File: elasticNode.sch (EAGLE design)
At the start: 135 parts, among them J1 FEMALE_HEADER_2X1, J2 JUMPER, J3 JUMPER, J5 FEMALE_HEADER_10X2, J6 USB_CONNMICRO_SMT, J7 USB_CONNMICRO_SMT, M1 SISS23DN, M2 SISS23DN, M3 SISS23DN, M4 SISS23DN, U1 AT90USB128, U10 LTC3419DFN, U11 PAC1720, U14 LTC3419DFN, U2 IS66WV51216EALL, U3 MRF24J40MA, U4 SPARTAN7-LX15, U5 ATMEGA32U4QFN, U6 SST26VF032BWDFN, U7 PAC1720, U8 PAC1720, U9 PAC1720, X1 8MHz, X2 50MHz, X3 32MHz, X4 100MHz, X5 8MHz

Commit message: backup
SRAM and FPGA finished, now connecting fpga and MCU
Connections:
- new net N$52: U4.IO_L15N_T2_DQS_DOUT_CSO_B_14
- net AD0/SELECTMAP_D7: no longer U4.IO_L5N_T0_D07_14
- net AD1/SELECTMAP_D6: no longer U4.IO_L5P_T0_D06_14
- net AD2/SELECTMAP_D5/MCU_RX1: no longer U4.IO_L4N_T0_D05_14
- net AD3/SELECTMAP_D4/MCU_TX1: no longer U4.IO_L4P_T0_D04_14
- net AD4/SELECTMAP_D3/FPGA_HOLD: no longer U4.IO_L2N_T0_D03_14
- net AD5/SELECTMAP_D2/FPGA_WP: no longer U4.IO_L2P_T0_D02_14
- net AD6/SELECTMAP_D1/SPI_MISO/MCU_PDO: no longer U4.IO_L1N_T0_D01_DIN_14
- net AD7/SELECTMAP_D0/SPI_MOSI/PDI: no longer U4.IO_L1P_T0_D00_MOSI_14
- net ALE/HWB: no longer U4.IO_L12P_T1_MRCC_14
- net FPGA_LED0: no longer U4.IO_0_14
- net FPGA_LED1: no longer U4.IO_L3P_T0_DQS_PUDC_B_14
- net FPGA_LED2: no longer U4.IO_L3N_T0_DQS_EMCCLK_14
- net FPGA_LED3: no longer U4.IO_L6N_T0_D08_VREF_14
- net SPI_CS: no longer U4.IO_L15N_T2_DQS_DOUT_CSO_B_14, U4.IO_L6P_T0_FCS_B_14
- net SRAM_A0: now also U4.IO_L5P_T0_34
- net SRAM_A1: now also U4.IO_L3P_T0_DQS_34
- net SRAM_A12: now also U4.IO_L24P_T3_34
- net SRAM_A13: now also U4.IO_L21P_T3_DQS_34
- net SRAM_A14: now also U4.IO_L21N_T3_DQS_34
- net SRAM_A15: now also U4.IO_L20P_T3_34
- net SRAM_A16: now also U4.IO_L17P_T2_34
- net SRAM_A2: now also U4.IO_L4P_T0_34
- net SRAM_A3: now also U4.IO_0_34
- net SRAM_CS: now also U4.IO_L6N_T0_VREF_34
- net SRAM_D0: now also U4.IO_L1N_T0_34
- net SRAM_D1: now also U4.IO_L10N_T1_34
- net SRAM_D2: now also U4.IO_L1P_T0_34
- net SRAM_D3: now also U4.IO_L10P_T1_34
- net SRAM_D4: now also U4.IO_L8N_T1_34
- net SRAM_D5: now also U4.IO_L8P_T1_34
- net SRAM_D6: now also U4.IO_L13P_T2_MRCC_34
- net SRAM_D7: now also U4.IO_L14P_T2_SRCC_34
- net SRAM_WE: now also U4.IO_L13N_T2_MRCC_34
- net XMEM_A10: now also U4.IO_L5P_T0_D06_14; no longer U4.IO_L10N_T1_D15_14
- net XMEM_A11: no longer U4.IO_L8N_T1_D12_14
- net XMEM_A12: now also U4.IO_L11N_T1_SRCC_14, U4.IO_L6N_T0_D08_VREF_14; no longer U4.IO_L9P_T1_DQS_14
- net XMEM_A13: now also U4.IO_L8P_T1_D11_14; no longer U4.IO_L9N_T1_DQS_D13_14
- net XMEM_A14: no longer U4.IO_L10P_T1_D14_14
- net XMEM_A15: no longer U4.IO_L7P_T1_D09_14
- net XMEM_A8: now also U4.IO_L1N_T0_D01_DIN_14; no longer U4.IO_L7N_T1_D10_14
- net XMEM_A9: now also U4.IO_L5N_T0_D07_14; no longer U4.IO_L8P_T1_D11_14
- net XMEM_RD: now also U4.IO_L4N_T0_D05_14; no longer U4.IO_L11N_T1_SRCC_14
- net XMEM_WR: now also U4.IO_L4P_T0_D04_14; no longer U4.IO_L11P_T1_SRCC_14

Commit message: back up
spi_sck didn’t connect to FPGA,OK？
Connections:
- net AD6/SELECTMAP_D1/SPI_MISO/MCU_PDO: now also U4.IO_L1N_T0_D01_DIN_14
- net AD7/SELECTMAP_D0/SPI_MOSI/PDI: now also U4.IO_L1P_T0_D00_MOSI_14
- net FPGA_LED0: now also U4.IO_L2P_T0_D02_14
- net FPGA_LED1: now also U4.IO_L2N_T0_D03_14
- net FPGA_LED2: now also U4.IO_L3P_T0_DQS_PUDC_B_14
- net FPGA_LED3: now also U4.IO_L3N_T0_DQS_EMCCLK_14
- net XMEM_A10: no longer U4.IO_L5P_T0_D06_14
- net XMEM_A12: no longer U4.IO_L11N_T1_SRCC_14, U4.IO_L6N_T0_D08_VREF_14
- net XMEM_A13: no longer U4.IO_L8P_T1_D11_14
- net XMEM_A8: no longer U4.IO_L1N_T0_D01_DIN_14
- net XMEM_A9: no longer U4.IO_L5N_T0_D07_14

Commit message: backup
SPI FLASH ok.
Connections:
- removed net N$52: U4.IO_L15N_T2_DQS_DOUT_CSO_B_14
- net AD0/SELECTMAP_D7: now also U4.IO_L5N_T0_D07_14
- net AD1/SELECTMAP_D6: now also U4.IO_L5P_T0_D06_14
- net AD2/SELECTMAP_D5/MCU_RX1: now also U4.IO_L4N_T0_D05_14
- net AD3/SELECTMAP_D4/MCU_TX1: now also U4.IO_L4P_T0_D04_14
- net AD4/SELECTMAP_D3/FPGA_HOLD: now also U4.IO_L2N_T0_D03_14
- net AD5/SELECTMAP_D2/FPGA_WP: now also U4.IO_L2P_T0_D02_14
- net FPGA_LED0: now also U4.IO_0_14; no longer U4.IO_L2P_T0_D02_14
- net FPGA_LED1: now also U4.IO_L3P_T0_DQS_PUDC_B_14; no longer U4.IO_L2N_T0_D03_14
- net FPGA_LED2: now also U4.IO_L3N_T0_DQS_EMCCLK_14; no longer U4.IO_L3P_T0_DQS_PUDC_B_14
- net FPGA_LED3: no longer U4.IO_L3N_T0_DQS_EMCCLK_14
- net SPI_CS: now also U4.IO_L6P_T0_FCS_B_14
- net XMEM_RD: no longer U4.IO_L4N_T0_D05_14
- net XMEM_WR: no longer U4.IO_L4P_T0_D04_14

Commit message: backup
FPGA_GPIO connecting
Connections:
- new net N$1: U4.IO_L24N_T3_D16_14
- new net N$31: U4.IO_L22N_T3_D20_14
- new net N$32: U4.IO_L22P_T3_D21_14
- new net N$35: U4.IO_L15N_T2_DQS_DOUT_CSO_B_14
- new net N$36: U4.IO_L21N_T3_DQS_D22_14
- new net N$37: U4.IO_L21P_T3_DQS_14
- new net N$8: U4.IO_L24P_T3_D17_14
- net ALE/HWB: now also U4.IO_L9P_T1_DQS_14
- net FPGA_GPIO_0: now also U4.IO_L13N_T2_MRCC_14; no longer U4.IO_L22N_T3_D20_14
- net FPGA_GPIO_1: no longer U4.IO_L22P_T3_D21_14
- net FPGA_GPIO_10: no longer U4.IO_25_14
- net FPGA_GPIO_11: now also U4.IO_L18P_T2_D28_14; no longer U4.IO_L16N_T2_D31_14
- net FPGA_GPIO_12: no longer U4.IO_L19N_T3_D25_VREF_14
- net FPGA_GPIO_13: now also U4.IO_L18N_T2_D27_14; no longer U4.IO_L19P_T3_D26_14
- net FPGA_GPIO_14: now also U4.IO_L19P_T3_D26_14; no longer U4.IO_L18N_T2_D27_14
- net FPGA_GPIO_15: no longer U4.IO_L18P_T2_D28_14
- net FPGA_GPIO_16: now also U4.IO_L19N_T3_D25_VREF_14; no longer U4.IO_L17N_T2_D29_14
- net FPGA_GPIO_17: no longer U4.IO_L17P_T2_D30_14
- net FPGA_GPIO_18: no longer U4.IO_L14N_T2_SRCC_14
- net FPGA_GPIO_19: no longer U4.IO_L14P_T2_SRCC_14
- net FPGA_GPIO_2: now also U4.IO_L14P_T2_SRCC_14; no longer U4.IO_L24N_T3_D16_14
- net FPGA_GPIO_3: no longer U4.IO_L24P_T3_D17_14
- net FPGA_GPIO_4: now also U4.IO_L14N_T2_SRCC_14; no longer U4.IO_L21P_T3_DQS_14
- net FPGA_GPIO_5: no longer U4.IO_L23N_T3_D18_14
- net FPGA_GPIO_6: now also U4.IO_L17P_T2_D30_14; no longer U4.IO_L23P_T3_D19_14
- net FPGA_GPIO_7: no longer U4.IO_L21N_T3_DQS_D22_14
- net FPGA_GPIO_8: now also U4.IO_L17N_T2_D29_14; no longer U4.IO_L20N_T3_D23_14
- net FPGA_GPIO_9: no longer U4.IO_L20P_T3_D24_14
- net FPGA_LED3: now also U4.IO_L6N_T0_D08_VREF_14
- net XMEM_A10: now also U4.IO_L7N_T1_D10_14
- net XMEM_A11: now also U4.IO_L10N_T1_D15_14
- net XMEM_A12: now also U4.IO_L7P_T1_D09_14
- net XMEM_A13: now also U4.IO_L10P_T1_D14_14
- net XMEM_A14: now also U4.IO_L9N_T1_DQS_D13_14
- net XMEM_A15: now also U4.IO_L12P_T1_MRCC_14
- net XMEM_A8: now also U4.IO_L8N_T1_D12_14
- net XMEM_A9: now also U4.IO_L11P_T1_SRCC_14
- net XMEM_RD: now also U4.IO_L8P_T1_D11_14
- net XMEM_WR: now also U4.IO_L11N_T1_SRCC_14

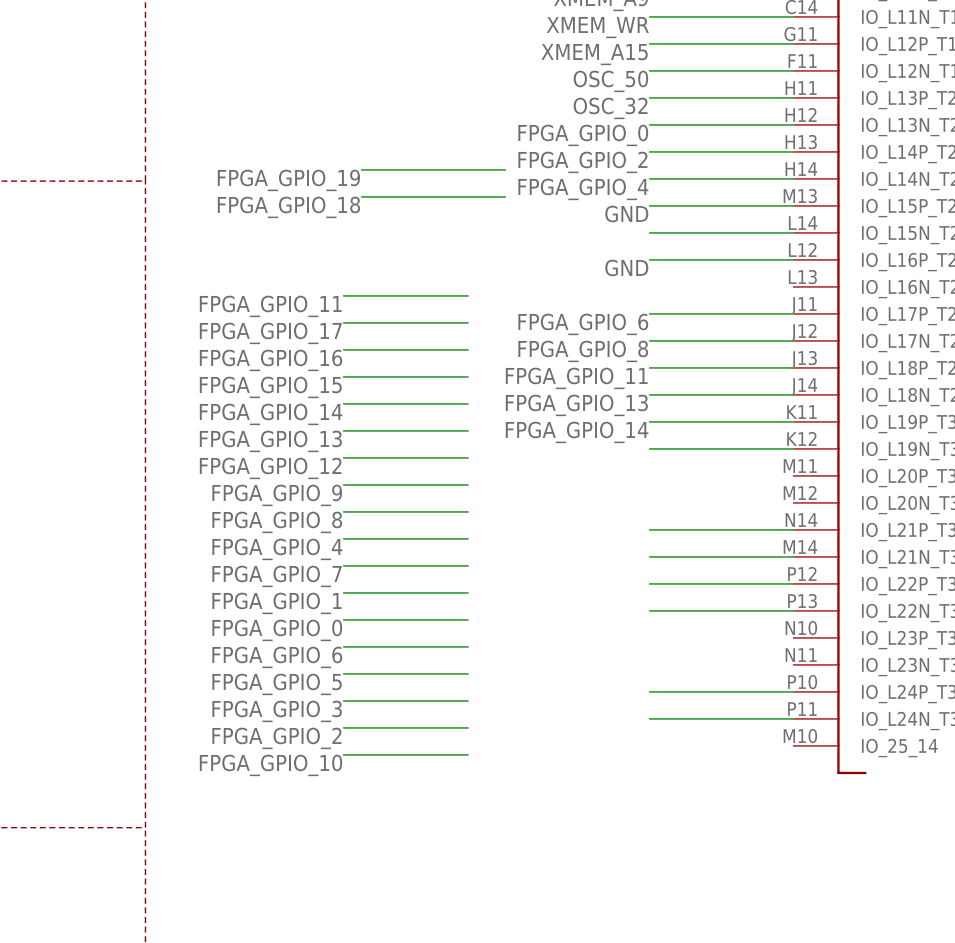
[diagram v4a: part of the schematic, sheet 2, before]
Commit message: back up
power line need check again.
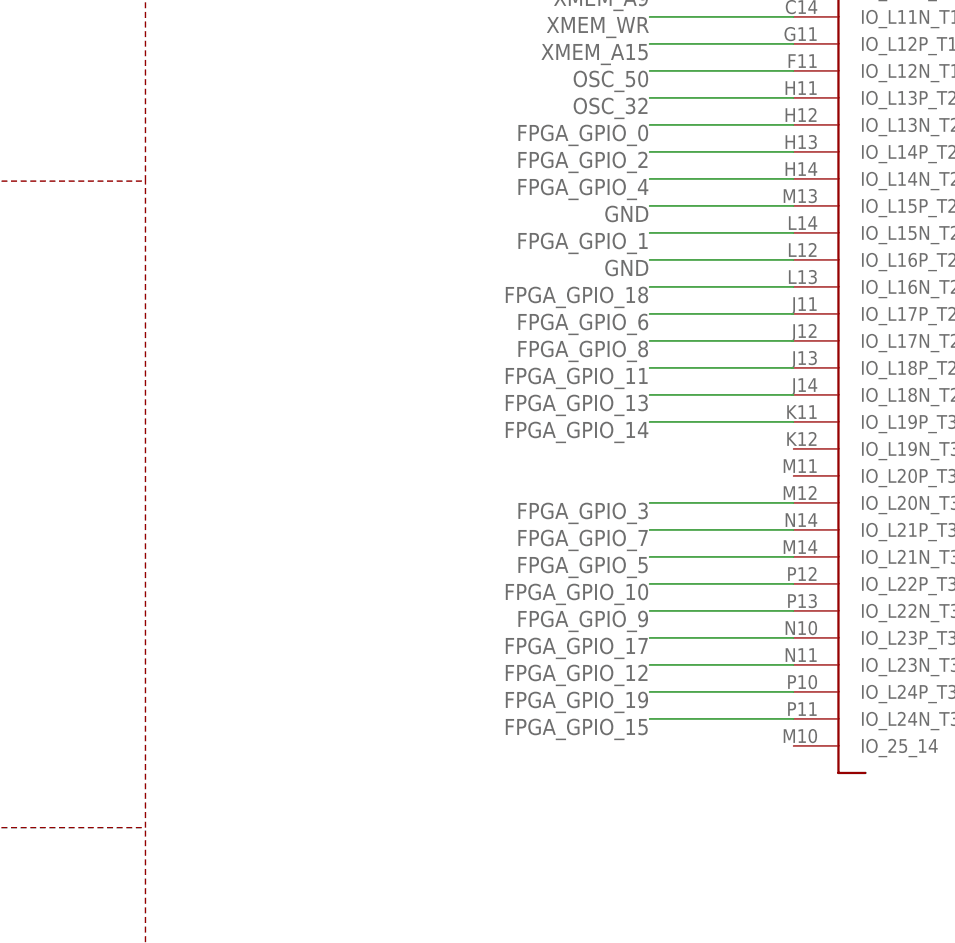
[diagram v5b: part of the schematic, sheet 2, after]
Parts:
- added R39: 2.4k, passive:RESISTOR
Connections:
- removed net N$1: U4.IO_L24N_T3_D16_14
- removed net N$31: U4.IO_L22N_T3_D20_14
- removed net N$32: U4.IO_L22P_T3_D21_14
- removed net N$35: U4.IO_L15N_T2_DQS_DOUT_CSO_B_14
- removed net N$36: U4.IO_L21N_T3_DQS_D22_14
- removed net N$37: U4.IO_L21P_T3_DQS_14
- removed net N$8: U4.IO_L24P_T3_D17_14
- net 3V3: now also R39.1
- net FPGA_GPIO_1: now also U4.IO_L15N_T2_DQS_DOUT_CSO_B_14
- net FPGA_GPIO_10: now also U4.IO_L22P_T3_D21_14
- net FPGA_GPIO_12: now also U4.IO_L23N_T3_D18_14
- net FPGA_GPIO_15: now also U4.IO_L24N_T3_D16_14
- net FPGA_GPIO_16: no longer U4.IO_L19N_T3_D25_VREF_14
- net FPGA_GPIO_17: now also U4.IO_L23P_T3_D19_14
- net FPGA_GPIO_18: now also U4.IO_L16N_T2_D31_14
- net FPGA_GPIO_19: now also U4.IO_L24P_T3_D17_14
- net FPGA_GPIO_3: now also U4.IO_L20N_T3_D23_14
- net FPGA_GPIO_5: now also U4.IO_L21N_T3_DQS_D22_14
- net FPGA_GPIO_7: now also U4.IO_L21P_T3_DQS_14
- net FPGA_GPIO_9: now also U4.IO_L22N_T3_D20_14
- net MONITORING: now also R39.2
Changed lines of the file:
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@@
 <part name="C30" library="passive" deviceset="CAPACITOR" device="0805" value="4.7u"/>
 <part name="C32" library="passive" deviceset="CAPACITOR" device="0805" value="0.47u"/>
+<part name="R39" library="passive" deviceset="RESISTOR" device="" value="2.4k"/>
 </parts>
 <sheets>
@@
 <attribute name="VALUE" x="9" y="-174" size="1.778" layer="96" align="top-center"/>
 </instance>
+<instance part="R39" gate="G$1" x="-141" y="-205" smashed="yes" rot="R90">
+<attribute name="NAME" x="-143" y="-205" size="1.778" layer="95" rot="R90" align="bottom-center"/>
+<attribute name="VALUE" x="-139" y="-205" size="1.778" layer="96" rot="R90" align="top-center"/>
+</instance>
 </instances>
 <busses>
@@
 <label x="169" y="-151" size="1.778" layer="95"/>
 </segment>
+<segment>
+<wire x1="-141" y1="-209.46" x2="-141" y2="-213" width="0.1524" layer="91"/>
+<label x="-141" y="-213" size="1.778" layer="95"/>
+<pinref part="R39" gate="G$1" pin="1"/>
+</segment>
 </net>
 <net name="INIT_B" class="0">
@@
 <segment>
 <pinref part="U5" gate="G$1" pin="PE6(INT6/AIN0)"/>
-<wire x1="-137" y1="-197" x2="-145" y2="-197" width="0.1524" layer="91"/>
 <label x="-145" y="-197" size="1.778" layer="95" rot="R180"/>
+<wire x1="-137" y1="-197" x2="-141" y2="-197" width="0.1524" layer="91"/>
+<wire x1="-141" y1="-197" x2="-145" y2="-197" width="0.1524" layer="91"/>
+<wire x1="-141" y1="-200.54" x2="-141" y2="-197" width="0.1524" layer="91"/>
+<junction x="-141" y="-197"/>
+<pinref part="R39" gate="G$1" pin="2"/>
 </segment>
 <segment>
@@
 </segment>
 <segment>
-<label x="-97" y="-62" size="1.778" layer="95" rot="R180"/>
-<wire x1="-83.1524" y1="-62" x2="-97" y2="-62" width="0.1524" layer="91"/>
-</segment>
-<segment>
 <pinref part="U4" gate="G$1" pin="IO_L13N_T2_MRCC_14"/>
 <wire x1="-47" y1="-7" x2="-63" y2="-7" width="0.1524" layer="91"/>
@@
 </segment>
 <segment>
-<label x="-97" y="-59" size="1.778" layer="95" rot="R180"/>
-<wire x1="-83.1524" y1="-59" x2="-97" y2="-59" width="0.1524" layer="91"/>
+<pinref part="U4" gate="G$1" pin="IO_L15N_T2_DQS_DOUT_CSO_B_14"/>
+<wire x1="-47" y1="-19" x2="-63" y2="-19" width="0.1524" layer="91"/>
+<label x="-63" y="-19" size="1.778" layer="95" rot="R180"/>
 </segment>
 </net>
@@
 </segment>
 <segment>
-<label x="-97" y="-74" size="1.778" layer="95" rot="R180"/>
-<wire x1="-83.1524" y1="-74" x2="-97" y2="-74" width="0.1524" layer="91"/>
-</segment>
-<segment>
 <pinref part="U4" gate="G$1" pin="IO_L14P_T2_SRCC_14"/>
 <wire x1="-47" y1="-10" x2="-63" y2="-10" width="0.1524" layer="91"/>
@@
 </segment>
 <segment>
-<label x="-97" y="-71" size="1.778" layer="95" rot="R180"/>
-<wire x1="-83.1524" y1="-71" x2="-97" y2="-71" width="0.1524" layer="91"/>
+<pinref part="U4" gate="G$1" pin="IO_L20N_T3_D23_14"/>
+<wire x1="-47" y1="-49" x2="-63" y2="-49" width="0.1524" layer="91"/>
+<label x="-63" y="-49" size="1.778" layer="95" rot="R180"/>
 </segment>
 </net>
@@
 </segment>
 <segment>
-<label x="-97" y="-53" size="1.778" layer="95" rot="R180"/>
-<wire x1="-83.1524" y1="-53" x2="-97" y2="-53" width="0.1524" layer="91"/>
-</segment>
-<segment>
 <pinref part="U4" gate="G$1" pin="IO_L14N_T2_SRCC_14"/>
 <wire x1="-47" y1="-13" x2="-63" y2="-13" width="0.1524" layer="91"/>
@@
 </segment>
 <segment>
-<label x="-97" y="-68" size="1.778" layer="95" rot="R180"/>
-<wire x1="-83.1524" y1="-68" x2="-97" y2="-68" width="0.1524" layer="91"/>
+<pinref part="U4" gate="G$1" pin="IO_L21N_T3_DQS_D22_14"/>
+<wire x1="-47" y1="-55" x2="-63" y2="-55" width="0.1524" layer="91"/>
+<label x="-63" y="-55" size="1.778" layer="95" rot="R180"/>
 </segment>
 </net>
@@
 </segment>
 <segment>
-<label x="-97" y="-65" size="1.778" layer="95" rot="R180"/>
-<wire x1="-83.1524" y1="-65" x2="-97" y2="-65" width="0.1524" layer="91"/>
-</segment>
-<segment>
 <pinref part="U4" gate="G$1" pin="IO_L17P_T2_D30_14"/>
 <wire x1="-47" y1="-28" x2="-63" y2="-28" width="0.1524" layer="91"/>
@@
 </segment>
 <segment>
-<label x="-97" y="-56" size="1.778" layer="95" rot="R180"/>
-<wire x1="-83.1524" y1="-56" x2="-97" y2="-56" width="0.1524" layer="91"/>
+<pinref part="U4" gate="G$1" pin="IO_L21P_T3_DQS_14"/>
+<wire x1="-47" y1="-52" x2="-63" y2="-52" width="0.1524" layer="91"/>
+<label x="-63" y="-52" size="1.778" layer="95" rot="R180"/>
 </segment>
 </net>
@@
 </segment>
 <segment>
-<label x="-97" y="-50" size="1.778" layer="95" rot="R180"/>
-<wire x1="-83.1524" y1="-50" x2="-97" y2="-50" width="0.1524" layer="91"/>
-</segment>
-<segment>
 <pinref part="U4" gate="G$1" pin="IO_L17N_T2_D29_14"/>
 <wire x1="-47" y1="-31" x2="-63" y2="-31" width="0.1524" layer="91"/>
@@
 </segment>
 <segment>
-<label x="-97" y="-47" size="1.778" layer="95" rot="R180"/>
-<wire x1="-83.1524" y1="-47" x2="-97" y2="-47" width="0.1524" layer="91"/>
+<pinref part="U4" gate="G$1" pin="IO_L22N_T3_D20_14"/>
+<wire x1="-47" y1="-61" x2="-63" y2="-61" width="0.1524" layer="91"/>
+<label x="-63" y="-61" size="1.778" layer="95" rot="R180"/>
 </segment>
 </net>
@@
 </segment>
 <segment>
-<label x="-97" y="-77" size="1.778" layer="95" rot="R180"/>
-<wire x1="-83.1524" y1="-77" x2="-97" y2="-77" width="0.1524" layer="91"/>
+<pinref part="U4" gate="G$1" pin="IO_L22P_T3_D21_14"/>
+<wire x1="-47" y1="-58" x2="-63" y2="-58" width="0.1524" layer="91"/>
+<label x="-63" y="-58" size="1.778" layer="95" rot="R180"/>
 </segment>
 </net>
@@
 </segment>
 <segment>
-<label x="-97" y="-26" size="1.778" layer="95" rot="R180"/>
-<wire x1="-83.1524" y1="-26" x2="-97" y2="-26" width="0.1524" layer="91"/>
-</segment>
-<segment>
 <pinref part="U4" gate="G$1" pin="IO_L18P_T2_D28_14"/>
 <wire x1="-47" y1="-34" x2="-63" y2="-34" width="0.1524" layer="91"/>
@@
 </segment>
 <segment>
-<label x="-97" y="-44" size="1.778" layer="95" rot="R180"/>
-<wire x1="-83.1524" y1="-44" x2="-97" y2="-44" width="0.1524" layer="91"/>
+<pinref part="U4" gate="G$1" pin="IO_L23N_T3_D18_14"/>
+<wire x1="-47" y1="-67" x2="-63" y2="-67" width="0.1524" layer="91"/>
+<label x="-63" y="-67" size="1.778" layer="95" rot="R180"/>
 </segment>
 </net>
@@
 </segment>
 <segment>
-<label x="-97" y="-41" size="1.778" layer="95" rot="R180"/>
-<wire x1="-83.1524" y1="-41" x2="-97" y2="-41" width="0.1524" layer="91"/>
-</segment>
-<segment>
 <pinref part="U4" gate="G$1" pin="IO_L18N_T2_D27_14"/>
 <wire x1="-47" y1="-37" x2="-63" y2="-37" width="0.1524" layer="91"/>
@@
 </segment>
 <segment>
-<label x="-97" y="-35" size="1.778" layer="95" rot="R180"/>
-<wire x1="-83.1524" y1="-35" x2="-97" y2="-35" width="0.1524" layer="91"/>
+<pinref part="U4" gate="G$1" pin="IO_L24N_T3_D16_14"/>
+<wire x1="-47" y1="-73" x2="-63" y2="-73" width="0.1524" layer="91"/>
+<label x="-63" y="-73" size="1.778" layer="95" rot="R180"/>
 </segment>
 </net>
@@
 </segment>
 <segment>
-<label x="-97" y="-29" size="1.778" layer="95" rot="R180"/>
-<wire x1="-83.1524" y1="-29" x2="-97" y2="-29" width="0.1524" layer="91"/>
+<pinref part="U4" gate="G$1" pin="IO_L23P_T3_D19_14"/>
+<wire x1="-47" y1="-64" x2="-63" y2="-64" width="0.1524" layer="91"/>
+<label x="-63" y="-64" size="1.778" layer="95" rot="R180"/>
 </segment>
 </net>
@@
 </segment>
 <segment>
-<wire x1="-79" y1="-12" x2="-95" y2="-12" width="0.1524" layer="91"/>
-<label x="-95" y="-12" size="1.778" layer="95" rot="R180"/>
+<pinref part="U4" gate="G$1" pin="IO_L24P_T3_D17_14"/>
+<wire x1="-47" y1="-70" x2="-63" y2="-70" width="0.1524" layer="91"/>
+<label x="-63" y="-70" size="1.778" layer="95" rot="R180"/>
 </segment>
 </net>
@@
 </segment>
 <segment>
-<wire x1="-79" y1="-15" x2="-95" y2="-15" width="0.1524" layer="91"/>
-<label x="-95" y="-15" size="1.778" layer="95" rot="R180"/>
+<pinref part="U4" gate="G$1" pin="IO_L16N_T2_D31_14"/>
+<wire x1="-47" y1="-25" x2="-63" y2="-25" width="0.1524" layer="91"/>
+<label x="-63" y="-25" size="1.778" layer="95" rot="R180"/>
 </segment>
 </net>
@@
 <label x="-210.36" y="0.66" size="1.778" layer="95" rot="R180"/>
 </segment>
-<segment>
-<label x="-97" y="-32" size="1.778" layer="95" rot="R180"/>
-<wire x1="-83.1524" y1="-32" x2="-97" y2="-32" width="0.1524" layer="91"/>
-</segment>
-<segment>
-<pinref part="U4" gate="G$1" pin="IO_L19N_T3_D25_VREF_14"/>
-<wire x1="-47" y1="-43" x2="-63" y2="-43" width="0.1524" layer="91"/>
-</segment>
 </net>
 <net name="FPGA_GPIO_14" class="0">
@@
 </segment>
 <segment>
-<label x="-97" y="-38" size="1.778" layer="95" rot="R180"/>
-<wire x1="-83.1524" y1="-38" x2="-97" y2="-38" width="0.1524" layer="91"/>
-</segment>
-<segment>
 <pinref part="U4" gate="G$1" pin="IO_L19P_T3_D26_14"/>
 <wire x1="-47" y1="-40" x2="-63" y2="-40" width="0.1524" layer="91"/>
@@
 </segment>
 </net>
-<net name="N$1" class="0">
-<segment>
-<pinref part="U4" gate="G$1" pin="IO_L24N_T3_D16_14"/>
-<wire x1="-47" y1="-73" x2="-63" y2="-73" width="0.1524" layer="91"/>
-</segment>
-</net>
-<net name="N$8" class="0">
-<segment>
-<pinref part="U4" gate="G$1" pin="IO_L24P_T3_D17_14"/>
-<wire x1="-47" y1="-70" x2="-63" y2="-70" width="0.1524" layer="91"/>
-</segment>
-</net>
-<net name="N$31" class="0">
-<segment>
-<pinref part="U4" gate="G$1" pin="IO_L22N_T3_D20_14"/>
-<wire x1="-47" y1="-61" x2="-63" y2="-61" width="0.1524" layer="91"/>
-</segment>
-</net>
-<net name="N$32" class="0">
-<segment>
-<pinref part="U4" gate="G$1" pin="IO_L22P_T3_D21_14"/>
-<wire x1="-47" y1="-58" x2="-63" y2="-58" width="0.1524" layer="91"/>
-</segment>
-</net>
-<net name="N$35" class="0">
-<segment>
-<pinref part="U4" gate="G$1" pin="IO_L15N_T2_DQS_DOUT_CSO_B_14"/>
-<wire x1="-47" y1="-19" x2="-63" y2="-19" width="0.1524" layer="91"/>
-</segment>
-</net>
-<net name="N$36" class="0">
-<segment>
-<pinref part="U4" gate="G$1" pin="IO_L21N_T3_DQS_D22_14"/>
-<wire x1="-47" y1="-55" x2="-63" y2="-55" width="0.1524" layer="91"/>
-</segment>
-</net>
-<net name="N$37" class="0">
-<segment>
-<pinref part="U4" gate="G$1" pin="IO_L21P_T3_DQS_14"/>
-<wire x1="-47" y1="-52" x2="-63" y2="-52" width="0.1524" layer="91"/>
-</segment>
-</net>

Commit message: only daughter board interface left
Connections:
- removed net GND1: D11.2, D12.2
- new net N$1: OUT1.9
- new net N$31: OUT1.8
- new net N$32: OUT1.7
- new net N$33: OUT1.6
- new net N$8: OUT1.10
- net AD0/SELECTMAP_D7: no longer OUT2.1
- net AD1/SELECTMAP_D6: no longer OUT2.2
- net AD2/SELECTMAP_D5/MCU_RX1: no longer OUT2.3
- net AD3/SELECTMAP_D4/MCU_TX1: no longer OUT2.4
- net AD4/SELECTMAP_D3/FPGA_HOLD: no longer OUT2.5
- net AD5/SELECTMAP_D2/FPGA_WP: no longer OUT2.6
- net ALE/HWB: no longer OUT1.9
- net FPGA_POWER: now also U1.(INT4/TOSC1)PE4; no longer U1.(SS/PCINT0)PB0
- net GND: now also D11.2, D12.2
- net MONITORING: no longer U1.(INT.6/AIN.0)PE6
- net SRAM_POWER: now also U1.(INT.5/TOSC2)PE5; no longer U1.(INT.7/AIN.1/UVCON)PE7
- net WIRELESS_CS: now also U1.(INT.6/AIN.0)PE6; no longer U1.PF1(ADC1)
- net WIRELESS_WAKE: now also U1.(PCINT7/OC.0A/OC.1C)PB7; no longer U1.(INT4/TOSC1)PE4
- net XMEM_A10: no longer OUT1.5
- net XMEM_A11: no longer OUT1.6
- net XMEM_A12: no longer OUT1.7
- net XMEM_A13: no longer OUT1.8
- net XMEM_A14: no longer OUT1.10
- net XMEM_A8: no longer OUT1.3
- net XMEM_A9: no longer OUT1.4
